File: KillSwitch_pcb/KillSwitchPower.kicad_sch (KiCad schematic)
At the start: 26 parts, among them SW3 SW_BATT, U2 AP7361C-33E, U4 AP7361C-33E, U6 MCP101-315D

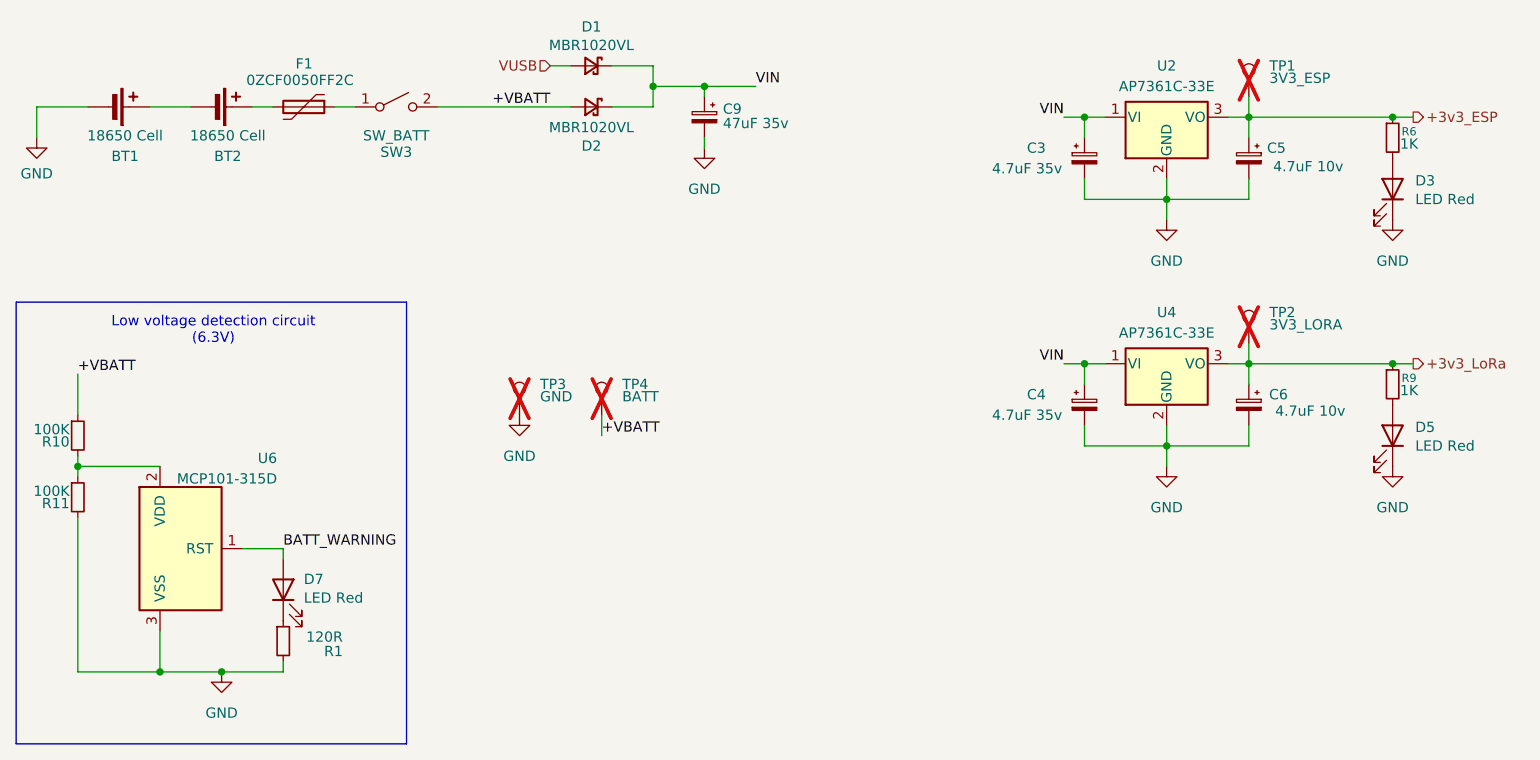
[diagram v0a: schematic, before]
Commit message: add pullups for i2c, reannotate, update footprints
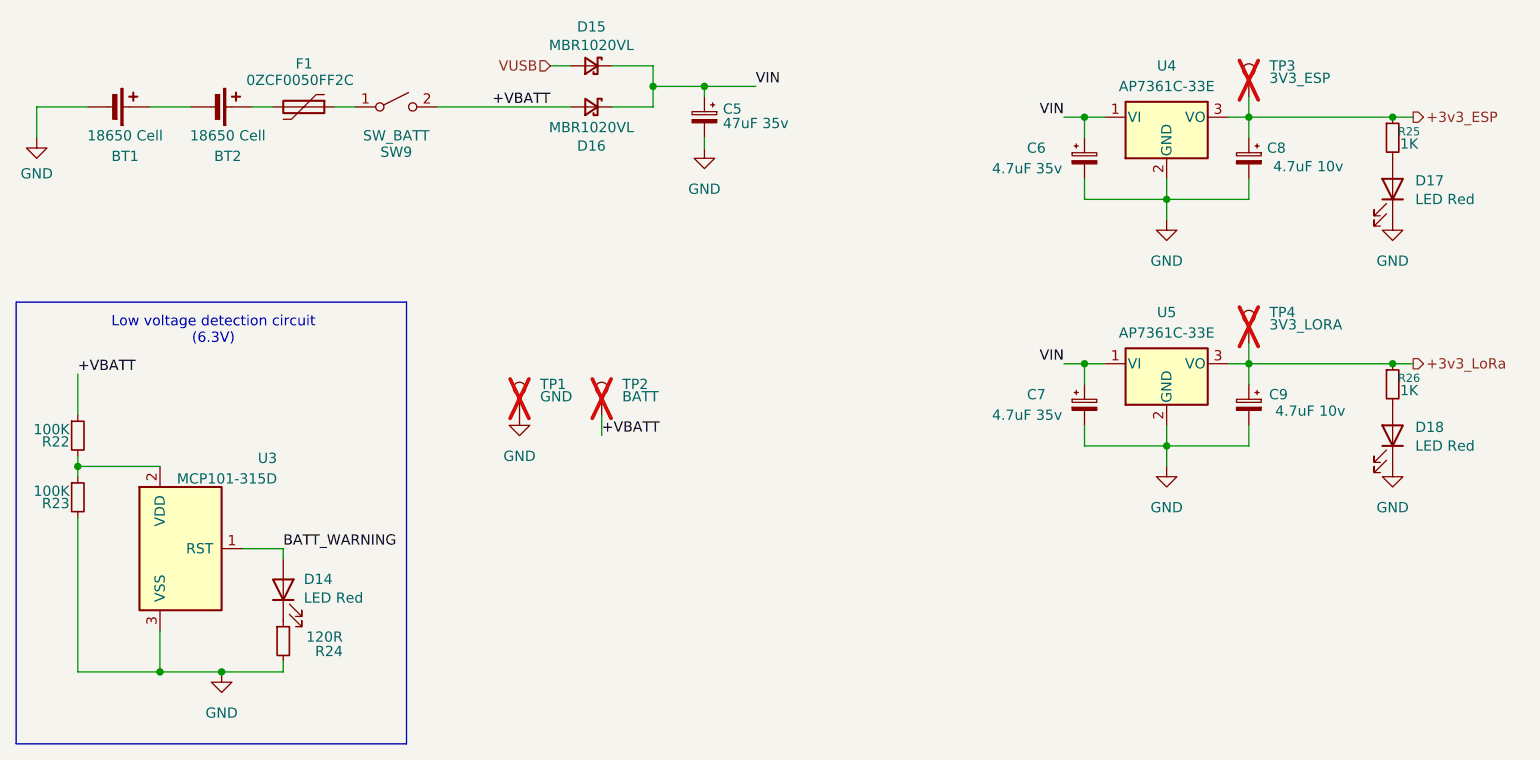
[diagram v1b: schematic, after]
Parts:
- renumbered C9 to C5, C3 to C6, C4 to C7, C5 to C8, C6 to C9, D7 to D14, D1 to D15, D2 to D16, D3 to D17, D5 to D18, R10 to R22, R11 to R23, R1 to R24, R6 to R25, R9 to R26, SW3 to SW9, TP3 to TP1, TP4 to TP2, TP1 to TP3, TP2 to TP4, U6 to U3, U2 to U4, U4 to U5

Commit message: update płytki: Routing bez GND plus obrys bez zaokrągleń i przycięć
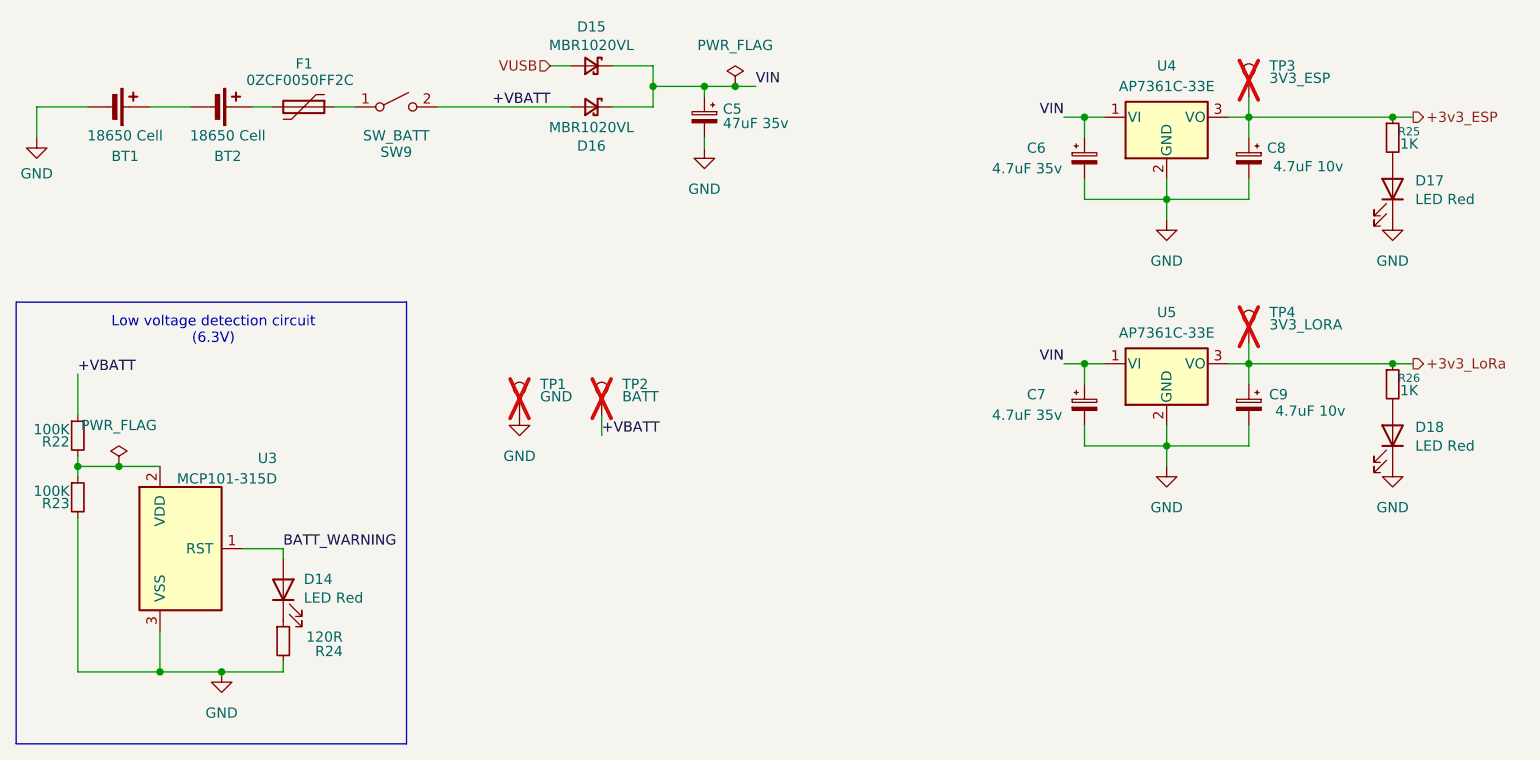
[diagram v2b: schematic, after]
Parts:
- R24: footprint Resistor_THT:R_Axial_DIN0204_L3.6mm_D1.6mm_P2.54mm_Vertical -> Resistor_SMD:R_0805_2012Metric_Pad1.20x1.40mm_HandSolder
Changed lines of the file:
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@@
+	)
+	(junction
+		(at 60.96 101.6)
+		(diameter 0)
+		(color 0 0 0 0)
+	)
+	(junction
+		(at 137.16 54.61)
+		(diameter 0)
+		(color 0 0 0 0)
 	)
 	(junction
@@
 	(wire
 		(pts
+			(xy 60.96 101.6) (xy 66.04 101.6)
+		)
+		(stroke
+			(width 0)
+			(type default)
+		)
+	)
+	(wire
+		(pts
 			(xy 200.66 55.88) (xy 200.66 58.42)
 		)
@@
 	(wire
 		(pts
-			(xy 66.04 101.6) (xy 55.88 101.6)
+			(xy 55.88 101.6) (xy 60.96 101.6)
 		)
 		(stroke
@@
 	(wire
 		(pts
+			(xy 137.16 54.61) (xy 139.7 54.61)
+		)
+		(stroke
+			(width 0)
+			(type default)
+		)
+	)
+	(wire
+		(pts
 			(xy 55.88 90.17) (xy 55.88 95.25)
 		)
@@
 	(wire
 		(pts
-			(xy 133.35 54.61) (xy 139.7 54.61)
+			(xy 133.35 54.61) (xy 137.16 54.61)
 		)
 		(stroke
@@
 			)
 		)
-		(property "Footprint" "Resistor_THT:R_Axial_DIN0204_L3.6mm_D1.6mm_P2.54mm_Vertical"
+		(property "Footprint" "Resistor_SMD:R_0805_2012Metric_Pad1.20x1.40mm_HandSolder"
 			(at 81.28 123.19 0)
 			(effects
@@
 	)
 	(symbol
+		(lib_id "power:PWR_FLAG")
+		(at 137.16 54.61 0)
+		(unit 1)
+		(exclude_from_sim no)
+		(in_bom yes)
+		(on_board yes)
+		(dnp no)
+		(fields_autoplaced yes)
+		(property "Reference" "#FLG01"
+			(at 137.16 52.705 0)
+			(effects
+				(font
+					(size 1.27 1.27)
+				)
+				(hide yes)
+			)
+		)
+		(property "Value" "PWR_FLAG"
+			(at 137.16 49.53 0)
+			(effects
+				(font
+					(size 1.27 1.27)
+				)
+			)
+		)
+		(property "Footprint" ""
+			(at 137.16 54.61 0)
+			(effects
+				(font
+					(size 1.27 1.27)
+				)
+				(hide yes)
+			)
+		)
+		(property "Datasheet" "~"
+			(at 137.16 54.61 0)
+			(effects
+				(font
+					(size 1.27 1.27)
+				)
+				(hide yes)
+			)
+		)
+		(property "Description" "Special symbol for telling ERC where power comes from"
+			(at 137.16 54.61 0)
+			(effects
+				(font
+					(size 1.27 1.27)
+				)
+				(hide yes)
+			)
+		)
+		(pin "1"
+		)
+		(instances
+			(project ""
+				(path "/722d8df3-08e9-470c-940d-01bb552f6a6b/b7784da9-1295-4ebc-bb4b-a445e94b65c1"
+					(reference "#FLG01")
+					(unit 1)
+				)
+			)
+		)
+	)
+	(symbol
 		(lib_id "Device:C_Polarized_Small")
 		(at 180.34 63.5 0)
@@
 					(unit 1)
 				)
+			)
+		)
+	)
+	(symbol
+		(lib_id "power:PWR_FLAG")
+		(at 60.96 101.6 0)
+		(unit 1)
+		(exclude_from_sim no)
+		(in_bom yes)
+		(on_board yes)
+		(dnp no)
+		(fields_autoplaced yes)
+		(property "Reference" "#FLG03"
+			(at 60.96 99.695 0)
+			(effects
+				(font
+					(size 1.27 1.27)
+				)
+				(hide yes)
+			)
+		)
+		(property "Value" "PWR_FLAG"
+			(at 60.96 96.52 0)
+			(effects
+				(font
+					(size 1.27 1.27)
+				)
+			)
+		)
+		(property "Footprint" ""
+			(at 60.96 101.6 0)
+			(effects
+				(font
+					(size 1.27 1.27)
+				)
+				(hide yes)
+			)
+		)
+		(property "Datasheet" "~"
+			(at 60.96 101.6 0)
+			(effects
+				(font
+					(size 1.27 1.27)
+				)
+				(hide yes)
+			)
+		)
+		(property "Description" "Special symbol for telling ERC where power comes from"
+			(at 60.96 101.6 0)
+			(effects
+				(font
+					(size 1.27 1.27)
+				)
+				(hide yes)
+			)
+		)
+		(pin "1"
+		)
+		(instances
+			(project "KillSwitch"
+				(path "/722d8df3-08e9-470c-940d-01bb552f6a6b/b7784da9-1295-4ebc-bb4b-a445e94b65c1"
+					(reference "#FLG03")
+					(unit 1)
+				)
